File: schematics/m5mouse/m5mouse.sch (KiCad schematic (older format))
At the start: 53 parts, among them IC1 LM3940IMP-3.3_NOPB, J1 Conn_01x02, J2 M-BUS, J3 SWD, J6 Conn_01x03, J7 Conn_01x06, J8 Conn_01x06, SW1 SW_SPDT, SW2 SW_Push, U1 TPS562200, U2 STM32F405RGTx, Y1 8MHz, Y2 32.768kHz

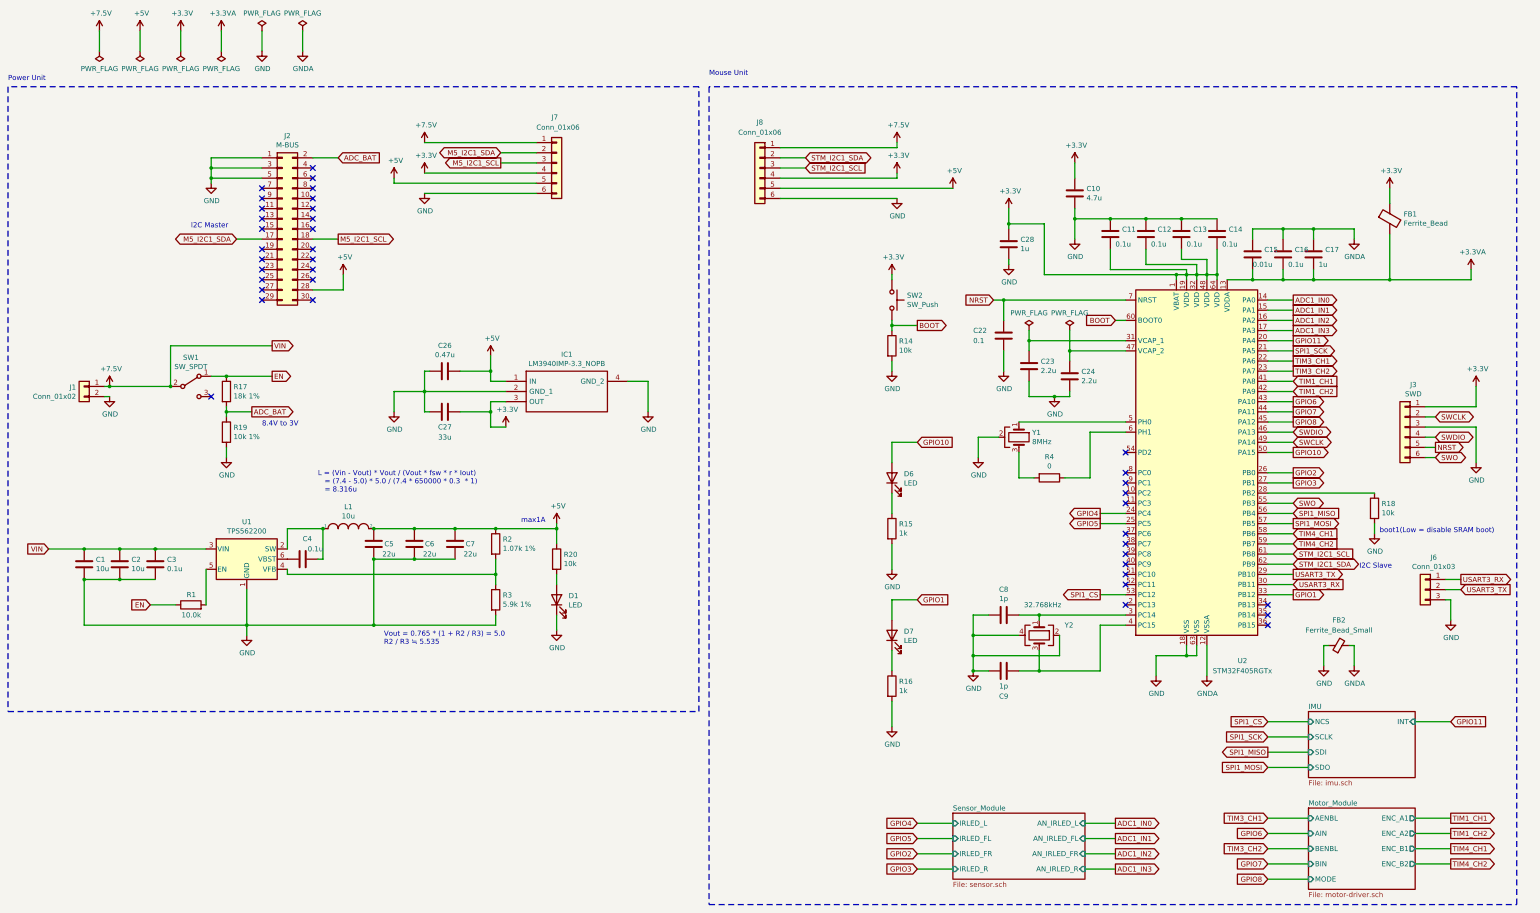
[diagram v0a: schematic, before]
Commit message: Fix schematics and patterns
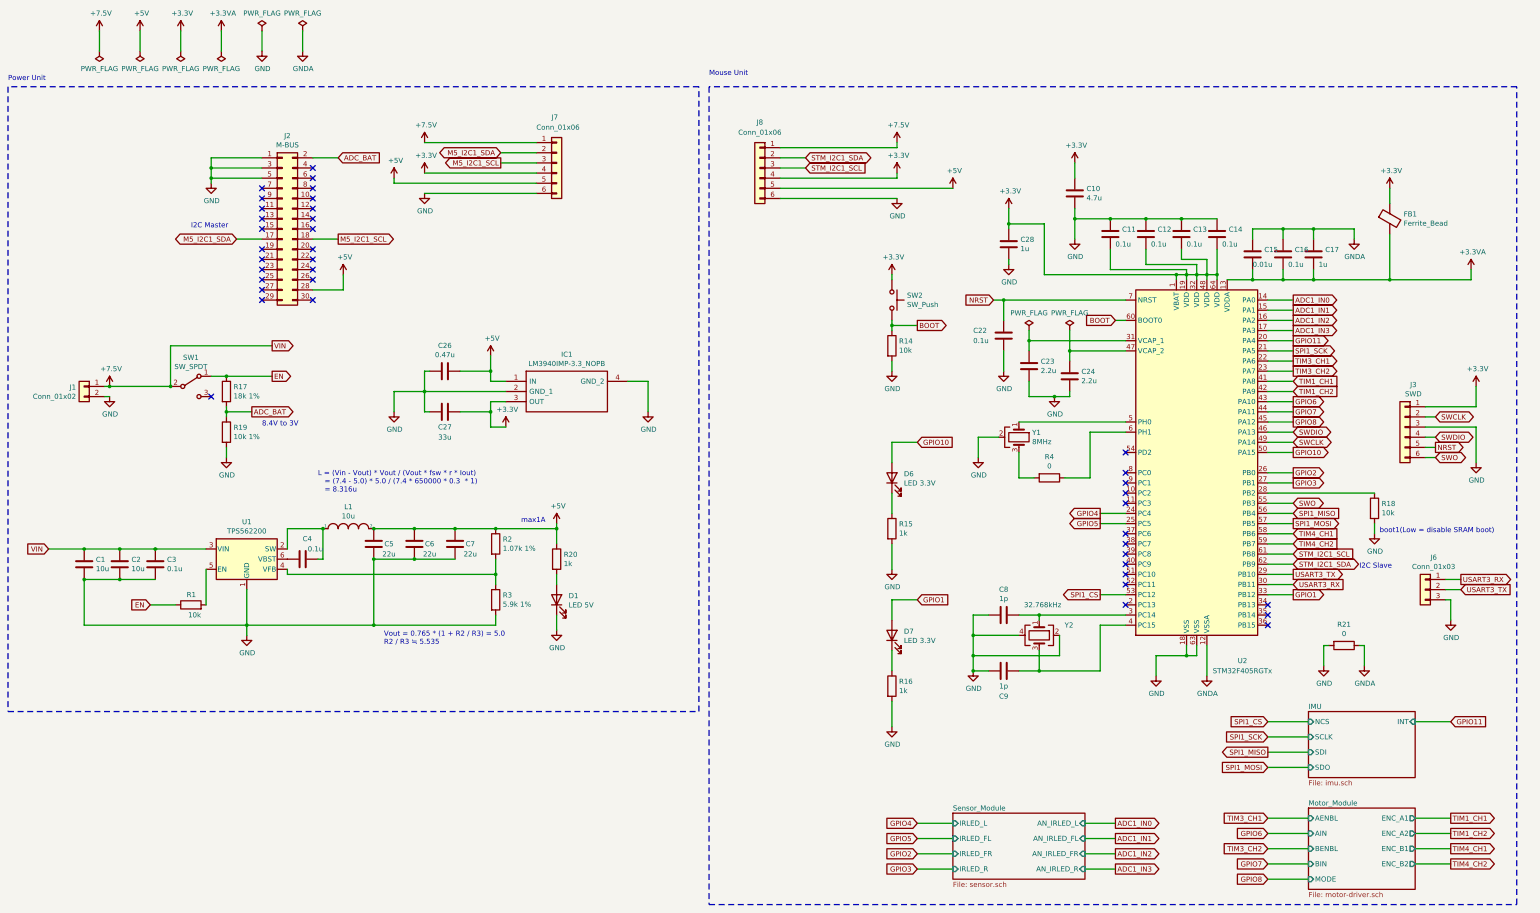
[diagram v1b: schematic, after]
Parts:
- removed FB2: Ferrite_Bead_Small, Resistor_SMD:R_0603_1608Metric, symbol Device:Ferrite_Bead_Small
- added R21: 0, Resistor_SMD:R_0603_1608Metric_Pad1.05x0.95mm_HandSolder, symbol Device:R
- C1: footprint Capacitor_SMD:C_0402_1005Metric -> Capacitor_SMD:C_0603_1608Metric; Manf# (none) -> GRM188R61A106KE69J; URL (none) -> https://www.digikey.jp/product-detail/ja/murata-electronics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
- C10: Manf# (none) -> GRM155R60J475ME87J; URL (none) -> https://www.digikey.jp/product-detail/ja/murata-electronics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
- C15: Manf# (none) -> C0402C103K8RACTU; URL (none) -> https://www.digikey.jp/product-detail/ja/kemet/C0402C103K8R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
- C17: Manf# (none) -> C0402C105K9PACTU; URL (none) -> https://www.digikey.jp/product-detail/ja/kemet/C0402C105K9P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
- C2: footprint Capacitor_SMD:C_0402_1005Metric -> Capacitor_SMD:C_0603_1608Metric
- C22: value 0.1 -> 0.1u
- C23: Manf# (none) -> GRM155R60J225ME15D; URL (none) -> https://www.digikey.jp/product-detail/ja/murata-electronics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
- C26: Manf# (none) -> CC0402KRX5R5BB474; URL (none) -> https://www.digikey.jp/product-detail/ja/yageo/CC0402KRX5R5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
- C27: footprint Capacitor_SMD:C_0402_1005Metric -> Capacitor_SMD:C_1206_3216Metric; Manf# (none) -> C3216X5R1A336M160AB; URL (none) -> https://www.digikey.jp/product-detail/ja/tdk-corporation/C3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
- C3: Manf# (none) -> CL05F104ZO5NNNC; URL (none) -> https://www.digikey.jp/product-detail/ja/samsung-electro-me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
- C5: footprint Capacitor_SMD:C_0402_1005Metric -> Capacitor_SMD:C_0805_2012Metric; Manf# (none) -> GRM21BR61A226ME51L; URL (none) -> https://www.digikey.jp/product-detail/ja/murata-electronics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
- C6, C7: footprint Capacitor_SMD:C_0402_1005Metric -> Capacitor_SMD:C_0805_2012Metric
- C8, C9: Manf# (none) -> CC0402CRNPO9BN1R0; URL (none) -> https://www.digikey.jp/product-detail/ja/yageo/CC0402CRNPO9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
- D1: value LED -> LED 5V; footprint LED_SMD:LED_0603_1608Metric -> LED_THT:LED_D3.0mm_Horizontal_O1.27mm_Z2.0mm; Manf# (none) -> WP710A10GD5V; URL (none) -> https://www.digikey.jp/product-detail/ja/kingbright/WP710A1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
- D6: value LED -> LED 3.3V; Manf# (none) -> LTST-C194TBKT; URL (none) -> https://www.digikey.jp/product-detail/ja/lite-on-inc/LTST-C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
- D7: value LED -> LED 3.3V
- FB1: footprint Resistor_SMD:R_0603_1608Metric -> Resistor_SMD:R_0402_1005Metric; Manf# (none) -> BLM15EG221SH1D; URL (none) -> https://www.digikey.jp/product-detail/ja/murata-electronics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
- IC1: Manf# (none) -> LM3940IMP-3.3/NOPB; URL (none) -> https://www.digikey.jp/product-detail/ja/texas-instruments/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
- J1: Manf# (none) -> B2B-PH-K-S(LF)(SN); URL (none) -> https://www.digikey.jp/product-detail/ja/jst-sales-america-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
- J2: Manf# (none) -> SKU: A001; URL (none) -> https://m5stack.com/collections/m5-accessory/products/2x15-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
- J3, J8: Manf# (none) -> 61300611121; URL (none) -> https://www.digikey.jp/product-detail/ja/w%C3%BCrth-elektro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
- J6: Manf# (none) -> 61300311121; URL (none) -> https://www.digikey.jp/product-detail/ja/w%C3%BCrth-elektro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
- J7: Manf# (none) -> PPPC061LFBN-RC; URL (none) -> https://www.digikey.jp/product-detail/ja/sullins-connector-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
- L1: Manf# (none) -> FIXED IND 10UH 1A 540 MOHM SMD; URL (none) -> https://www.digikey.jp/product-detail/ja/tdk-corporation/VL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
- R1: value 10.0k -> 10k; Manf# (none) -> RC0603FR-0710KL; URL (none) -> https://www.digikey.jp/product-detail/ja/yageo/RC0603FR-071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
- R14, R19: Manf# (none) -> RC0603FR-0710KL; URL (none) -> https://www.digikey.jp/product-detail/ja/yageo/RC0603FR-071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
- R15, R16: Manf# (none) -> RC0603FR-071KL; URL (none) -> https://www.digikey.jp/product-detail/ja/yageo/RC0603FR-071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
- R17: Manf# (none) -> CRGCQ0603F18K; URL (none) -> https://www.digikey.jp/product-detail/ja/te-connectivity-pa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
- R2: Manf# (none) -> RC0603FR-071K07L; URL (none) -> https://www.digikey.jp/product-detail/ja/yageo/RC0603FR-071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
- R20: value 10k -> 1k
- R3: Manf# (none) -> RC0603FR-075K9L; URL (none) -> https://www.digikey.jp/product-detail/ja/yageo/RC0603FR-075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
- R4: Manf# (none) -> RC0603JR-070RL; URL (none) -> https://www.digikey.jp/product-detail/ja/yageo/RC0603JR-070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
- SW1: Manf# (none) -> EG1224; URL (none) -> https://www.digikey.jp/product-detail/ja/e-switch/EG1224/EG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
- SW2: Manf# (none) -> 1825910-7; URL (none) -> https://www.digikey.jp/product-detail/ja/te-connectivity-al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
- U1: Manf# (none) -> TPS562200DDCR; URL (none) -> https://www.digikey.jp/product-detail/ja/texas-instruments/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
- U2: Manf# (none) -> STM32F405RGT7TR; URL (none) -> https://www.digikey.jp/product-detail/ja/stmicroelectronics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
- Y1: Manf# (none) -> CSTNE8M00G55Z000R0; URL (none) -> https://www.digikey.jp/product-detail/ja/murata-electronics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
- Y2: Manf# (none) -> XRCGB32M768F2N10R0; URL (none) -> https://www.digikey.jp/products/ja?keywords=XRCGB32M768F2N1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
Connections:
- net GND: now also R21.2
- net GNDA: now also R21.1

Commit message: Fix pattern
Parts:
- C8, C9: footprint Capacitor_SMD:C_0402_1005Metric -> Capacitor_SMD:C_0201_0603Metric; Manf# CC0402CRNPO9BN1R0 -> GRM0335C1H1R0CA01D; URL https://www.digikey.jp/product-detail/ja/yageo/CC0402CRNPO9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 -> https://www.digikey.jp/product-detail/ja/murata-electronics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
- J3: footprint Connector_JST:JST_EH_B6B-EH-A_1x06_P2.50mm_Vertical -> Connector_JST:JST_EH_S6B-EH_1x06_P2.50mm_Horizontal; Manf# 61300611121 -> B6B-EH-A; URL https://www.digikey.jp/product-detail/ja/w%C3%BCrth-elektro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 -> https://www.digikey.jp/product-detail/ja/jst-sales-america-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
- Y2: footprint m5mouse:XRCGB32M768F2N10R0 -> m5mouse:WMRAG32K76CS3C00R0; Manf# XRCGB32M768F2N10R0 -> WMRAG32K76CS3C00R0; URL https://www.digikey.jp/products/ja?keywords=XRCGB32M768F2N1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 -> https://www.digikey.jp/product-detail/ja/murata-electronics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
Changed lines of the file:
@@
 F 0 "Y2" V 10650 7350 50  0000 L CNN
 F 1 "32.768kHz" V 10450 6950 50  0000 L CNN
-F 2 "m5mouse:XRCGB32M768F2N10R0" H 10750 7100 50  0001 C CNN
+F 2 "m5mouse:WMRAG32K76CS3C00R0" H 10750 7100 50  0001 C CNN
 F 3 "~" H 10750 7100 50  0001 C CNN
-F 4 "XRCGB32M768F2N10R0" V 10750 7100 50  0001 C CNN "Manf#"
-F 5 "https://www.digikey.jp/products/ja?keywords=XRCGB32M768F2N10R0" V 10750 7100 50  0001 C CNN "URL"
+F 4 "WMRAG32K76CS3C00R0" V 10750 7100 50  0001 C CNN "Manf#"
+F 5 "https://www.digikey.jp/product-detail/ja/murata-electronics/WMRAG32K76CS3C00R0/490-WMRAG32K76CS3C00R0CT-ND/10406083" V 10750 7100 50  0001 C CNN "URL"
 	1    10750 7100
 	0    1    1    0
@@
 F 0 "C9" V 10650 7450 50  0000 C CNN
 F 1 "1p" V 10550 7450 50  0000 C CNN
-F 2 "Capacitor_SMD:C_0402_1005Metric" H 10438 7300 50  0001 C CNN
+F 2 "Capacitor_SMD:C_0201_0603Metric" H 10438 7300 50  0001 C CNN
 F 3 "~" H 10400 7450 50  0001 C CNN
-F 4 "CC0402CRNPO9BN1R0" V 10400 7450 50  0001 C CNN "Manf#"
-F 5 "https://www.digikey.jp/product-detail/ja/yageo/CC0402CRNPO9BN1R0/311-2076-1-ND/5252385" V 10400 7450 50  0001 C CNN "URL"
+F 4 "GRM0335C1H1R0CA01D" V 10400 7450 50  0001 C CNN "Manf#"
+F 5 "https://www.digikey.jp/product-detail/ja/murata-electronics/GRM0335C1H1R0CA01D/490-6118-1-ND/3845318" V 10400 7450 50  0001 C CNN "URL"
 	1    10400 7450
 	0    1    1    0
@@
 F 0 "C8" V 10148 6900 50  0000 C CNN
 F 1 "1p" V 10239 6900 50  0000 C CNN
-F 2 "Capacitor_SMD:C_0402_1005Metric" H 10438 6750 50  0001 C CNN
+F 2 "Capacitor_SMD:C_0201_0603Metric" H 10438 6750 50  0001 C CNN
 F 3 "~" H 10400 6900 50  0001 C CNN
-F 4 "CC0402CRNPO9BN1R0" V 10400 6900 50  0001 C CNN "Manf#"
-F 5 "https://www.digikey.jp/product-detail/ja/yageo/CC0402CRNPO9BN1R0/311-2076-1-ND/5252385" V 10400 6900 50  0001 C CNN "URL"
+F 4 "GRM0335C1H1R0CA01D" V 10400 6900 50  0001 C CNN "Manf#"
+F 5 "https://www.digikey.jp/product-detail/ja/murata-electronics/GRM0335C1H1R0CA01D/490-6118-1-ND/3845318" V 10400 6900 50  0001 C CNN "URL"
 	1    10400 6900
 	0    1    1    0
@@
 F 0 "J3" H 14268 5467 50  0000 C CNN
 F 1 "SWD" H 14268 5376 50  0000 C CNN
-F 2 "Connector_JST:JST_EH_B6B-EH-A_1x06_P2.50mm_Vertical" H 14350 5050 50  0001 C CNN
+F 2 "Connector_JST:JST_EH_S6B-EH_1x06_P2.50mm_Horizontal" H 14350 5050 50  0001 C CNN
 F 3 "~" H 14350 5050 50  0001 C CNN
-F 4 "https://www.digikey.jp/product-detail/ja/w%C3%BCrth-elektronik/61300611121/732-5319-ND/4846833" H 14350 5050 50  0001 C CNN "URL"
-F 5 "61300611121" H 14350 5050 50  0001 C CNN "Manf#"
+F 4 "https://www.digikey.jp/product-detail/ja/jst-sales-america-inc/B6B-EH-A/455-1018-ND/527242" H 14350 5050 50  0001 C CNN "URL"
+F 5 "B6B-EH-A" H 14350 5050 50  0001 C CNN "Manf#"
 	1    14350 5050
 	-1   0    0    -1

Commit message: Change ferrite bead
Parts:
- FB1: footprint Resistor_SMD:R_0402_1005Metric -> Resistor_SMD:R_0603_1608Metric; Manf# BLM15EG221SH1D -> MZ1608-102Y; URL https://www.digikey.jp/product-detail/ja/murata-electronics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 -> https://www.digikey.jp/product-detail/ja/bourns-inc/MZ1608-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
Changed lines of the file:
@@
 F 0 "FB1" H 14337 3046 50  0000 L CNN
 F 1 "Ferrite_Bead" H 14337 2955 50  0000 L CNN
-F 2 "Resistor_SMD:R_0402_1005Metric" V 14130 3000 50  0001 C CNN
+F 2 "Resistor_SMD:R_0603_1608Metric" V 14130 3000 50  0001 C CNN
 F 3 "~" H 14200 3000 50  0001 C CNN
-F 4 "BLM15EG221SH1D" H 14200 3000 50  0001 C CNN "Manf#"
-F 5 "https://www.digikey.jp/product-detail/ja/murata-electronics/BLM15EG221SH1D/490-17345-1-ND/7798458" H 14200 3000 50  0001 C CNN "URL"
+F 4 "MZ1608-102Y" H 14200 3000 50  0001 C CNN "Manf#"
+F 5 "https://www.digikey.jp/product-detail/ja/bourns-inc/MZ1608-102Y/MZ1608-102YCT-ND/3767848" H 14200 3000 50  0001 C CNN "URL"
 	1    14200 3000
 	1    0    0    -1
